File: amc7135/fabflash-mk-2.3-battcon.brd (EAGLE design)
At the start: 22 x 22 mm, 3 parts

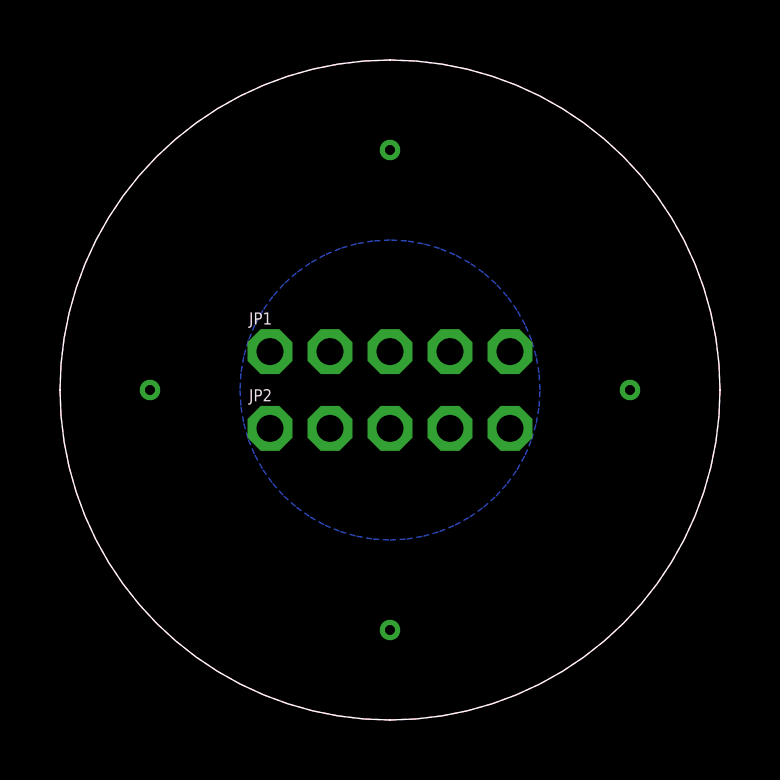
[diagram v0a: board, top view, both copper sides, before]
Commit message: batt con plate to smd, controller with isp using jst-zh con
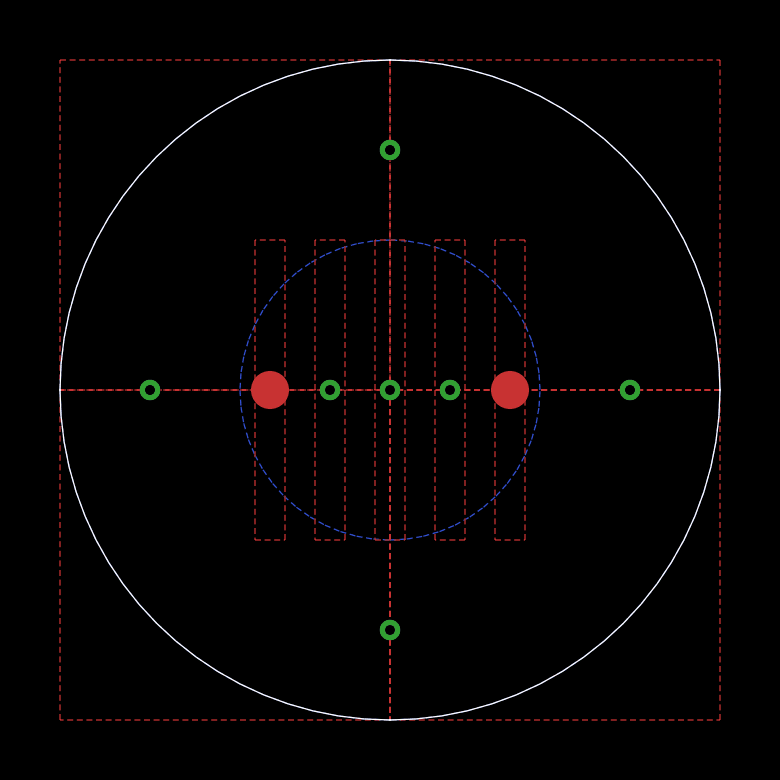
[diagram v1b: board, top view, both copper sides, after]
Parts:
- removed JP1: (no value), A_butts:1X05-0.9X2MM-PTH
- added JP4, JP5: M01NOT-A-VIA-NOPE, A_butts:1X01_NOSILK_NOSTOP
- added JP6, JP7: M01NOSTOP-CANTSTOP-DONTKNOWHOWTOSTOP, A_butts:1X01_SMD_NOSTOP_NOSILK
- JP2: value (none) -> M01NOT-A-VIA-NOPE; device A_butts:1X05-0.9X2MM-PTH -> A_butts:1X01_NOSILK_NOSTOP
- moved JP2 1.28 mm to (11.0, 11.0)
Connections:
- net GND: now also JP6.1, JP7.1; no longer JP1.1, JP1.5, JP2.1, JP2.5
- net VIN: now also JP2.P$1, JP4.P$1, JP5.P$1; no longer JP1.2, JP1.3, JP1.4, JP2.2, JP2.3, JP2.4
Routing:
- added copper zone on layer 1, net VIN
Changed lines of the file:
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@@
 <elements>
 <element name="JP3" library="A_butts" package="1X01_NOSILK_NOSTOP" value="M01NOT-A-VIA-NOPE" x="11" y="3"/>
-<element name="JP1" library="A_butts" package="1X05-0.9X2MM-PTH" value="" x="11" y="12.28"/>
-<element name="JP2" library="A_butts" package="1X05-0.9X2MM-PTH" value="" x="11" y="9.72"/>
+<element name="JP2" library="A_butts" package="1X01_NOSILK_NOSTOP" value="M01NOT-A-VIA-NOPE" x="11" y="11"/>
+<element name="JP4" library="A_butts" package="1X01_NOSILK_NOSTOP" value="M01NOT-A-VIA-NOPE" x="9" y="11"/>
+<element name="JP5" library="A_butts" package="1X01_NOSILK_NOSTOP" value="M01NOT-A-VIA-NOPE" x="13" y="11"/>
+<element name="JP6" library="A_butts" package="1X01_SMD_NOSTOP_NOSILK" value="M01NOSTOP-CANTSTOP-DONTKNOWHOWTOSTOP" x="15" y="11" smashed="yes"/>
+<element name="JP7" library="A_butts" package="1X01_SMD_NOSTOP_NOSILK" value="M01NOSTOP-CANTSTOP-DONTKNOWHOWTOSTOP" x="7" y="11" smashed="yes"/>
 </elements>
 <signals>
 <signal name="VIN">
-<polygon width="0.1524" layer="16">
+<polygon width="0.1524" layer="16" isolate="0.254">
 <vertex x="6" y="11" curve="90"/>
 <vertex x="11" y="6" curve="90"/>
@@
 <vertex x="11" y="16" curve="90"/>
 </polygon>
-<contactref element="JP1" pad="2"/>
-<contactref element="JP1" pad="3"/>
-<contactref element="JP1" pad="4"/>
-<contactref element="JP2" pad="2"/>
-<contactref element="JP2" pad="3"/>
-<contactref element="JP2" pad="4"/>
+<contactref element="JP2" pad="P$1"/>
+<contactref element="JP4" pad="P$1"/>
+<contactref element="JP5" pad="P$1"/>
+<polygon width="0.1524" layer="1">
+<vertex x="10.5" y="16"/>
+<vertex x="10.5" y="6"/>
+<vertex x="11.5" y="6"/>
+<vertex x="11.5" y="16"/>
+</polygon>
+<polygon width="0.1524" layer="1">
+<vertex x="12.5" y="16"/>
+<vertex x="13.5" y="16"/>
+<vertex x="13.5" y="6"/>
+<vertex x="12.5" y="6"/>
+</polygon>
+<polygon width="0.1524" layer="1">
+<vertex x="9.5" y="16"/>
+<vertex x="8.5" y="16"/>
+<vertex x="8.5" y="6"/>
+<vertex x="9.5" y="6"/>
+</polygon>
 </signal>
 <signal name="GND">
-<contactref element="JP3" pad="P$1"/>
-<polygon width="0.1524" layer="1">
-<vertex x="11" y="0" curve="-90"/>
-<vertex x="0" y="11" curve="-90"/>
-<vertex x="11" y="22" curve="-90"/>
-<vertex x="22" y="11" curve="-90"/>
-</polygon>
-<polygon width="0.1524" layer="16" rank="2">
+<polygon width="0.1524" layer="16" isolate="0.254" rank="6">
 <vertex x="11" y="0" curve="-90"/>
 <vertex x="0" y="11" curve="-90"/>
@@
 <via x="3" y="11" extent="1-16" drill="0.3324"/>
 <via x="19" y="11" extent="1-16" drill="0.3324"/>
-<contactref element="JP2" pad="5"/>
-<contactref element="JP2" pad="1"/>
-<contactref element="JP1" pad="1"/>
-<contactref element="JP1" pad="5"/>
+<contactref element="JP6" pad="1"/>
+<contactref element="JP7" pad="1"/>
+<polygon width="0.1524" layer="1">
+<vertex x="14.5" y="16"/>
+<vertex x="14.5" y="6"/>
+<vertex x="15.5" y="6"/>
+<vertex x="15.5" y="16"/>
+</polygon>
+<polygon width="0.1524" layer="1" isolate="0.254">
+<vertex x="7.5" y="16"/>
+<vertex x="6.5" y="16"/>
+<vertex x="6.5" y="6"/>
+<vertex x="7.5" y="6"/>
+</polygon>
+<polygon width="0.1524" layer="1" rank="6">
+<vertex x="0" y="11"/>
+<vertex x="0" y="22"/>
+<vertex x="11" y="22"/>
+<vertex x="11" y="11"/>
+</polygon>
+<polygon width="0.1524" layer="1" rank="6">
+<vertex x="0" y="0"/>
+<vertex x="0" y="11"/>
+<vertex x="11" y="11"/>
+<vertex x="11" y="0"/>
+</polygon>
+<polygon width="0.1524" layer="1" rank="6">
+<vertex x="11" y="11"/>
+<vertex x="11" y="0"/>
+<vertex x="22" y="0"/>
+<vertex x="22" y="11"/>
+</polygon>
+<polygon width="0.1524" layer="1" rank="6">
+<vertex x="11" y="22"/>
+<vertex x="22" y="22"/>
+<vertex x="22" y="11"/>
+<vertex x="11" y="11"/>
+</polygon>
+<contactref element="JP3" pad="P$1"/>
+<wire x1="3" y1="11" x2="7" y2="11" width="0" layer="19" extent="1-1"/>
+<wire x1="15" y1="11" x2="19" y2="11" width="0" layer="19" extent="1-1"/>
 </signal>
 </signals>

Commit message: added #2 screw holes to each board and verified pins aligned correctly (had to flipflop 5v/gnd a few times)
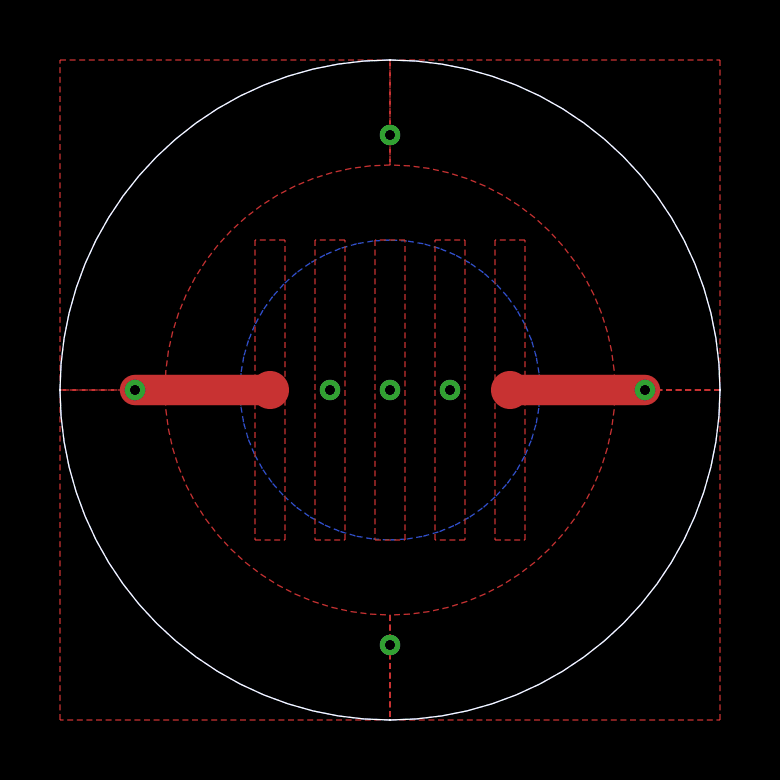
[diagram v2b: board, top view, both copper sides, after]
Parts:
- moved JP3 0.50 mm to (11.0, 2.50)
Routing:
- net GND: track 0.00 -> 9.00 mm
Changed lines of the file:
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@@
 <wire x1="22" y1="11" x2="11" y2="22" width="0" layer="20" curve="90"/>
 <wire x1="11" y1="22" x2="0" y2="11" width="0" layer="20" curve="90"/>
-<circle x="11" y="11" radius="10.2" width="1.6" layer="29"/>
 <circle x="11" y="11" radius="10.2" width="1.6" layer="30"/>
+<circle x="11" y="11" radius="9.2" width="3.55" layer="29"/>
 <circle x="11" y="11" radius="5.1" width="0" layer="30"/>
+<polygon width="0.1524" layer="29">
+<vertex x="6.4" y="16.1"/>
+<vertex x="6.4" y="5.9"/>
+<vertex x="7.6" y="5.9"/>
+<vertex x="7.6" y="16.1"/>
+</polygon>
+<polygon width="0.1524" layer="29">
+<vertex x="8.4" y="16.1"/>
+<vertex x="8.4" y="5.9"/>
+<vertex x="9.6" y="5.9"/>
+<vertex x="9.6" y="16.1"/>
+</polygon>
+<polygon width="0.1524" layer="29">
+<vertex x="10.4" y="16.1"/>
+<vertex x="10.4" y="5.9"/>
+<vertex x="11.6" y="5.9"/>
+<vertex x="11.6" y="16.1"/>
+</polygon>
+<polygon width="0.1524" layer="29">
+<vertex x="12.4" y="16.1"/>
+<vertex x="12.4" y="5.9"/>
+<vertex x="13.6" y="5.9"/>
+<vertex x="13.6" y="16.1"/>
+</polygon>
+<polygon width="0.1524" layer="29">
+<vertex x="14.4" y="16.1"/>
+<vertex x="14.4" y="5.9"/>
+<vertex x="15.6" y="5.9"/>
+<vertex x="15.6" y="16.1"/>
+</polygon>
 </plain>
 <attributes>
@@
 </autorouter>
 <elements>
-<element name="JP3" library="A_butts" package="1X01_NOSILK_NOSTOP" value="M01NOT-A-VIA-NOPE" x="11" y="3"/>
+<element name="JP3" library="A_butts" package="1X01_NOSILK_NOSTOP" value="M01NOT-A-VIA-NOPE" x="11" y="2.5"/>
 <element name="JP2" library="A_butts" package="1X01_NOSILK_NOSTOP" value="M01NOT-A-VIA-NOPE" x="11" y="11"/>
 <element name="JP4" library="A_butts" package="1X01_NOSILK_NOSTOP" value="M01NOT-A-VIA-NOPE" x="9" y="11"/>
@@
 <vertex x="22" y="11" curve="-90"/>
 </polygon>
-<via x="11" y="19" extent="1-16" drill="0.3324"/>
-<via x="3" y="11" extent="1-16" drill="0.3324"/>
-<via x="19" y="11" extent="1-16" drill="0.3324"/>
+<via x="11" y="19.5" extent="1-16" drill="0.3324"/>
+<via x="2.5" y="11" extent="1-16" drill="0.3324"/>
+<via x="19.5" y="11" extent="1-16" drill="0.3324"/>
 <contactref element="JP6" pad="1"/>
 <contactref element="JP7" pad="1"/>
-<polygon width="0.1524" layer="1">
+<polygon width="0.1524" layer="1" thermals="no">
 <vertex x="14.5" y="16"/>
 <vertex x="14.5" y="6"/>
@@
 <vertex x="15.5" y="16"/>
 </polygon>
-<polygon width="0.1524" layer="1" isolate="0.254">
+<polygon width="0.1524" layer="1" isolate="0.254" thermals="no">
 <vertex x="7.5" y="16"/>
 <vertex x="6.5" y="16"/>
@@
 <vertex x="0" y="22"/>
 <vertex x="11" y="22"/>
-<vertex x="11" y="11"/>
+<vertex x="11" y="18.5" curve="90"/>
+<vertex x="3.5" y="11"/>
 </polygon>
 <polygon width="0.1524" layer="1" rank="6">
 <vertex x="0" y="0"/>
 <vertex x="0" y="11"/>
-<vertex x="11" y="11"/>
+<vertex x="3.5" y="11" curve="90"/>
+<vertex x="11" y="3.5"/>
 <vertex x="11" y="0"/>
 </polygon>
 <polygon width="0.1524" layer="1" rank="6">
-<vertex x="11" y="11"/>
+<vertex x="11" y="3.5"/>
 <vertex x="11" y="0"/>
 <vertex x="22" y="0"/>
 <vertex x="22" y="11"/>
+<vertex x="18.5" y="11" curve="-90"/>
 </polygon>
 <polygon width="0.1524" layer="1" rank="6">
@@
 <vertex x="22" y="22"/>
 <vertex x="22" y="11"/>
-<vertex x="11" y="11"/>
+<vertex x="18.5" y="11" curve="90"/>
+<vertex x="11" y="18.5"/>
 </polygon>
 <contactref element="JP3" pad="P$1"/>
-<wire x1="3" y1="11" x2="7" y2="11" width="0" layer="19" extent="1-1"/>
-<wire x1="15" y1="11" x2="19" y2="11" width="0" layer="19" extent="1-1"/>
+<wire x1="7" y1="11" x2="2.5" y2="11" width="1.016" layer="1"/>
+<wire x1="15" y1="11" x2="19.5" y2="11" width="1.016" layer="1"/>
 </signal>
 </signals>

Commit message: revised batt con plate to remove any gnd traces from near the bottom spring connector. this will mean a cobbled together 4x header for the top side, but whatever
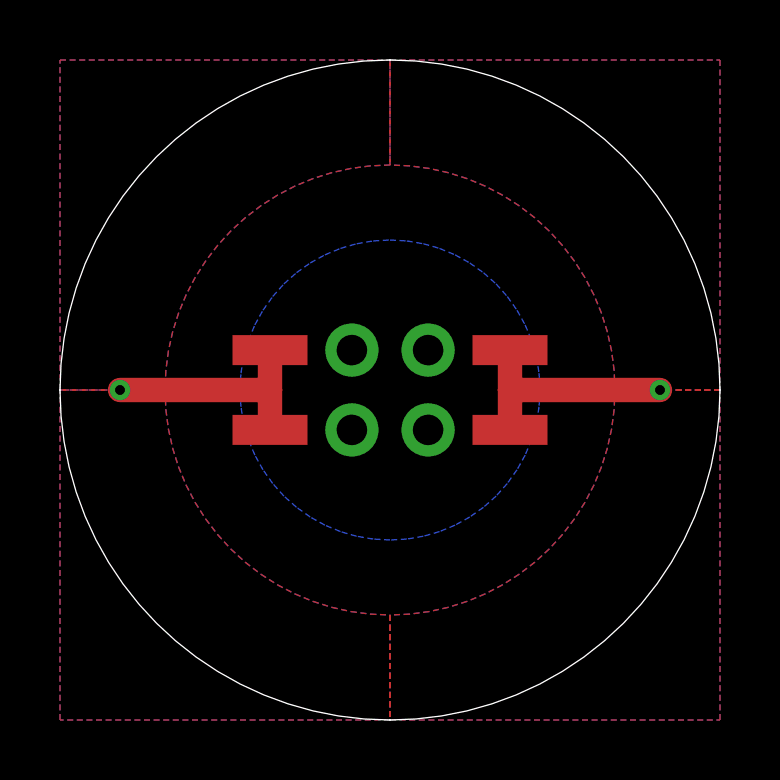
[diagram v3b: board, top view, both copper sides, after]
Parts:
- added JP1: M01NOT-A-VIA-NOPE, A_butts:1X01_NOSILK_NOSTOP
- added JP10: M01SMD-1X2.5MM-NS, A_butts:1X01-SMD-1X2.5MM-NS
- added JP8, JP9: M01NOSILK-KIT, A_butts:1X01NS-KIT
- JP3: value M01NOT-A-VIA-NOPE -> M01SMD-1X2.5MM-NS; device A_butts:1X01_NOSILK_NOSTOP -> A_butts:1X01-SMD-1X2.5MM-NS
- JP4, JP5: value M01NOT-A-VIA-NOPE -> M01NOSILK-KIT; device A_butts:1X01_NOSILK_NOSTOP -> A_butts:1X01NS-KIT
- JP6, JP7: value M01NOSTOP-CANTSTOP-DONTKNOWHOWTOSTOP -> M01SMD-1X2.5MM-NS; device A_butts:1X01_SMD_NOSTOP_NOSILK -> A_butts:1X01-SMD-1X2.5MM-NS
- moved JP3 10.6 mm to (7.00, 12.3), turned to 270 degrees
- moved JP2 9.00 mm to (20.0, 11.0)
- moved JP4 3.53 mm to (12.3, 12.3), turned to 90 degrees
- moved JP5 3.53 mm to (9.73, 12.3), turned to 90 degrees
- moved JP6 1.33 mm to (15.0, 12.3), turned to 90 degrees
- moved JP7 1.33 mm to (7.00, 9.67), turned to 270 degrees
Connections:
- net GND: now also JP1.P$1, JP10.1, JP2.P$1, JP3.1; no longer JP3.P$1
- net VIN: now also JP4.1, JP5.1, JP8.1, JP9.1; no longer JP2.P$1, JP4.P$1, JP5.P$1
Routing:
- net GND: track 9.00 -> 15.3 mm, vias 3 -> 0
- removed copper zone on layer 1, net VIN
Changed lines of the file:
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@@
 <setting verticaltext="up"/>
 </settings>
-<grid distance="0.5" unitdist="mm" unit="mm" style="lines" multiple="1" display="yes" altdistance="1" altunitdist="mil" altunit="mil"/>
+<grid distance="0.25" unitdist="mm" unit="mm" style="lines" multiple="1" display="yes" altdistance="1" altunitdist="mil" altunit="mil"/>
 <layers>
 <layer number="1" name="Top" color="4" fill="1" visible="yes" active="yes"/>
@@
 <wire x1="22" y1="11" x2="11" y2="22" width="0" layer="20" curve="90"/>
 <wire x1="11" y1="22" x2="0" y2="11" width="0" layer="20" curve="90"/>
-<circle x="11" y="11" radius="10.2" width="1.6" layer="30"/>
-<circle x="11" y="11" radius="9.2" width="3.55" layer="29"/>
-<circle x="11" y="11" radius="5.1" width="0" layer="30"/>
-<polygon width="0.1524" layer="29">
-<vertex x="6.4" y="16.1"/>
-<vertex x="6.4" y="5.9"/>
-<vertex x="7.6" y="5.9"/>
-<vertex x="7.6" y="16.1"/>
-</polygon>
-<polygon width="0.1524" layer="29">
-<vertex x="8.4" y="16.1"/>
-<vertex x="8.4" y="5.9"/>
-<vertex x="9.6" y="5.9"/>
-<vertex x="9.6" y="16.1"/>
-</polygon>
-<polygon width="0.1524" layer="29">
-<vertex x="10.4" y="16.1"/>
-<vertex x="10.4" y="5.9"/>
-<vertex x="11.6" y="5.9"/>
-<vertex x="11.6" y="16.1"/>
-</polygon>
-<polygon width="0.1524" layer="29">
-<vertex x="12.4" y="16.1"/>
-<vertex x="12.4" y="5.9"/>
-<vertex x="13.6" y="5.9"/>
-<vertex x="13.6" y="16.1"/>
-</polygon>
-<polygon width="0.1524" layer="29">
-<vertex x="14.4" y="16.1"/>
-<vertex x="14.4" y="5.9"/>
-<vertex x="15.6" y="5.9"/>
-<vertex x="15.6" y="16.1"/>
-</polygon>
+<circle x="11" y="11" radius="9.2" width="3.55" layer="30"/>
+<polygon width="0.5" layer="29">
+<vertex x="1" y="16"/>
+<vertex x="5.5" y="16" curve="-50"/>
+<vertex x="11" y="18.5" curve="-50"/>
+<vertex x="16.5" y="16"/>
+<vertex x="21" y="16" curve="60"/>
+<vertex x="11" y="22" curve="60"/>
+</polygon>
+<polygon width="0.5" layer="29">
+<vertex x="21" y="6"/>
+<vertex x="16.5" y="6" curve="-50"/>
+<vertex x="11" y="3.5" curve="-50"/>
+<vertex x="5.5" y="6"/>
+<vertex x="1" y="6" curve="60"/>
+<vertex x="11" y="0" curve="60"/>
+</polygon>
+<circle x="11" y="11" radius="5.2" width="0" layer="30"/>
 </plain>
 <attributes>
@@
 </autorouter>
 <elements>
-<element name="JP3" library="A_butts" package="1X01_NOSILK_NOSTOP" value="M01NOT-A-VIA-NOPE" x="11" y="2.5"/>
-<element name="JP2" library="A_butts" package="1X01_NOSILK_NOSTOP" value="M01NOT-A-VIA-NOPE" x="11" y="11"/>
-<element name="JP4" library="A_butts" package="1X01_NOSILK_NOSTOP" value="M01NOT-A-VIA-NOPE" x="9" y="11"/>
-<element name="JP5" library="A_butts" package="1X01_NOSILK_NOSTOP" value="M01NOT-A-VIA-NOPE" x="13" y="11"/>
-<element name="JP6" library="A_butts" package="1X01_SMD_NOSTOP_NOSILK" value="M01NOSTOP-CANTSTOP-DONTKNOWHOWTOSTOP" x="15" y="11" smashed="yes"/>
-<element name="JP7" library="A_butts" package="1X01_SMD_NOSTOP_NOSILK" value="M01NOSTOP-CANTSTOP-DONTKNOWHOWTOSTOP" x="7" y="11" smashed="yes"/>
+<element name="JP1" library="A_butts" package="1X01_NOSILK_NOSTOP" value="M01NOT-A-VIA-NOPE" x="2" y="11"/>
+<element name="JP2" library="A_butts" package="1X01_NOSILK_NOSTOP" value="M01NOT-A-VIA-NOPE" x="20" y="11"/>
+<element name="JP5" library="A_butts" package="1X01NS-KIT" value="M01NOSILK-KIT" x="9.73" y="12.33" rot="R90"/>
+<element name="JP3" library="A_butts" package="1X01-SMD-1X2.5MM-NS" value="M01SMD-1X2.5MM-NS" x="7" y="12.33" rot="R270"/>
+<element name="JP4" library="A_butts" package="1X01NS-KIT" value="M01NOSILK-KIT" x="12.27" y="12.33" rot="R90"/>
+<element name="JP6" library="A_butts" package="1X01-SMD-1X2.5MM-NS" value="M01SMD-1X2.5MM-NS" x="15" y="12.33" rot="R90"/>
+<element name="JP7" library="A_butts" package="1X01-SMD-1X2.5MM-NS" value="M01SMD-1X2.5MM-NS" x="7" y="9.67" rot="R270"/>
+<element name="JP8" library="A_butts" package="1X01NS-KIT" value="M01NOSILK-KIT" x="9.73" y="9.67" rot="R270"/>
+<element name="JP9" library="A_butts" package="1X01NS-KIT" value="M01NOSILK-KIT" x="12.27" y="9.67" rot="R270"/>
+<element name="JP10" library="A_butts" package="1X01-SMD-1X2.5MM-NS" value="M01SMD-1X2.5MM-NS" x="15" y="9.67" rot="R90"/>
 </elements>
 <signals>
 <signal name="VIN">
-<polygon width="0.1524" layer="16" isolate="0.254">
-<vertex x="6" y="11" curve="90"/>
-<vertex x="11" y="6" curve="90"/>
-<vertex x="16" y="11" curve="90"/>
-<vertex x="11" y="16" curve="90"/>
-</polygon>
-<contactref element="JP2" pad="P$1"/>
-<contactref element="JP4" pad="P$1"/>
-<contactref element="JP5" pad="P$1"/>
-<polygon width="0.1524" layer="1">
-<vertex x="10.5" y="16"/>
-<vertex x="10.5" y="6"/>
-<vertex x="11.5" y="6"/>
-<vertex x="11.5" y="16"/>
-</polygon>
-<polygon width="0.1524" layer="1">
-<vertex x="12.5" y="16"/>
-<vertex x="13.5" y="16"/>
-<vertex x="13.5" y="6"/>
-<vertex x="12.5" y="6"/>
-</polygon>
-<polygon width="0.1524" layer="1">
-<vertex x="9.5" y="16"/>
-<vertex x="8.5" y="16"/>
-<vertex x="8.5" y="6"/>
-<vertex x="9.5" y="6"/>
+<contactref element="JP5" pad="1"/>
+<contactref element="JP4" pad="1"/>
+<contactref element="JP9" pad="1"/>
+<contactref element="JP8" pad="1"/>
+<polygon width="0.1524" layer="16">
+<vertex x="11" y="6" curve="-90"/>
+<vertex x="6" y="11" curve="-90"/>
+<vertex x="11" y="16" curve="-90"/>
+<vertex x="16" y="11" curve="-90"/>
 </polygon>
 </signal>
 <signal name="GND">
-<polygon width="0.1524" layer="16" isolate="0.254" rank="6">
-<vertex x="11" y="0" curve="-90"/>
-<vertex x="0" y="11" curve="-90"/>
-<vertex x="11" y="22" curve="-90"/>
-<vertex x="22" y="11" curve="-90"/>
-</polygon>
-<via x="11" y="19.5" extent="1-16" drill="0.3324"/>
-<via x="2.5" y="11" extent="1-16" drill="0.3324"/>
-<via x="19.5" y="11" extent="1-16" drill="0.3324"/>
-<contactref element="JP6" pad="1"/>
-<contactref element="JP7" pad="1"/>
-<polygon width="0.1524" layer="1" thermals="no">
-<vertex x="14.5" y="16"/>
-<vertex x="14.5" y="6"/>
-<vertex x="15.5" y="6"/>
-<vertex x="15.5" y="16"/>
-</polygon>
-<polygon width="0.1524" layer="1" isolate="0.254" thermals="no">
-<vertex x="7.5" y="16"/>
-<vertex x="6.5" y="16"/>
-<vertex x="6.5" y="6"/>
-<vertex x="7.5" y="6"/>
-</polygon>
 <polygon width="0.1524" layer="1" rank="6">
 <vertex x="0" y="11"/>
@@
 <vertex x="11" y="18.5"/>
 </polygon>
-<contactref element="JP3" pad="P$1"/>
-<wire x1="7" y1="11" x2="2.5" y2="11" width="1.016" layer="1"/>
-<wire x1="15" y1="11" x2="19.5" y2="11" width="1.016" layer="1"/>
+<contactref element="JP1" pad="P$1"/>
+<contactref element="JP2" pad="P$1"/>
+<polygon width="0.1524" layer="16" rank="6">
+<vertex x="0" y="11"/>
+<vertex x="0" y="22"/>
+<vertex x="11" y="22"/>
+<vertex x="11" y="18.5" curve="90"/>
+<vertex x="3.5" y="11"/>
+</polygon>
+<polygon width="0.1524" layer="16" rank="6">
+<vertex x="11" y="22"/>
+<vertex x="22" y="22"/>
+<vertex x="22" y="11"/>
+<vertex x="18.5" y="11" curve="90"/>
+<vertex x="11" y="18.5"/>
+</polygon>
+<polygon width="0.1524" layer="16" rank="6">
+<vertex x="11" y="3.5"/>
+<vertex x="11" y="0"/>
+<vertex x="22" y="0"/>
+<vertex x="22" y="11"/>
+<vertex x="18.5" y="11" curve="-90"/>
+</polygon>
+<polygon width="0.1524" layer="16" rank="6">
+<vertex x="0" y="0"/>
+<vertex x="0" y="11"/>
+<vertex x="3.5" y="11" curve="90"/>
+<vertex x="11" y="3.5"/>
+<vertex x="11" y="0"/>
+</polygon>
+<contactref element="JP6" pad="1"/>
+<contactref element="JP3" pad="1"/>
+<contactref element="JP7" pad="1"/>
+<contactref element="JP10" pad="1"/>
+<wire x1="7" y1="9.67" x2="7" y2="11" width="0.8128" layer="1"/>
+<wire x1="7" y1="11" x2="7" y2="12.33" width="0.8128" layer="1"/>
+<wire x1="15" y1="9.67" x2="15" y2="11" width="0.8128" layer="1"/>
+<wire x1="15" y1="11" x2="15" y2="12.33" width="0.8128" layer="1"/>
+<wire x1="20" y1="11" x2="15" y2="11" width="0.8128" layer="1"/>
+<wire x1="2" y1="11" x2="7" y2="11" width="0.8128" layer="1"/>
 </signal>
 </signals>
